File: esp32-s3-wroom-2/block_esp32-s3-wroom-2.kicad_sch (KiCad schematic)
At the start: 11 parts, among them SW1 SW_Push, SW2 SW_Push, U1 ESP32-S3-WROOM-2

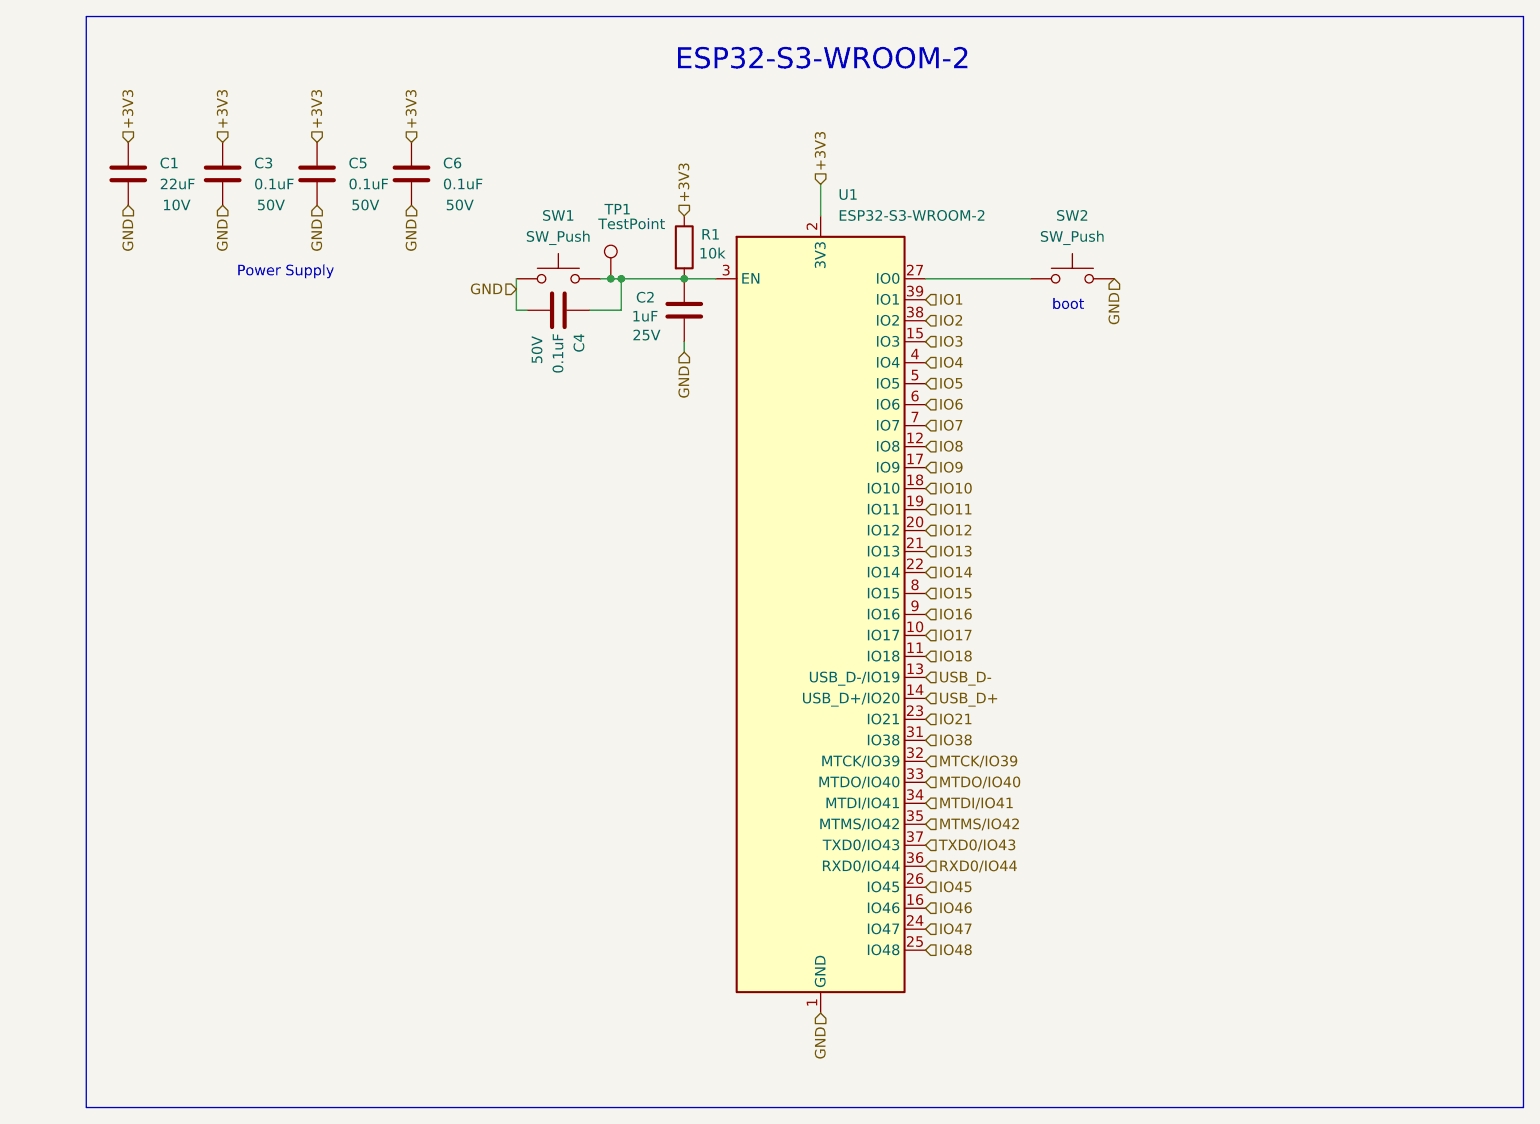
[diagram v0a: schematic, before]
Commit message: [Rushil] corrected pcb added information on both schematic and pcb user drawing correct circuit of bno055
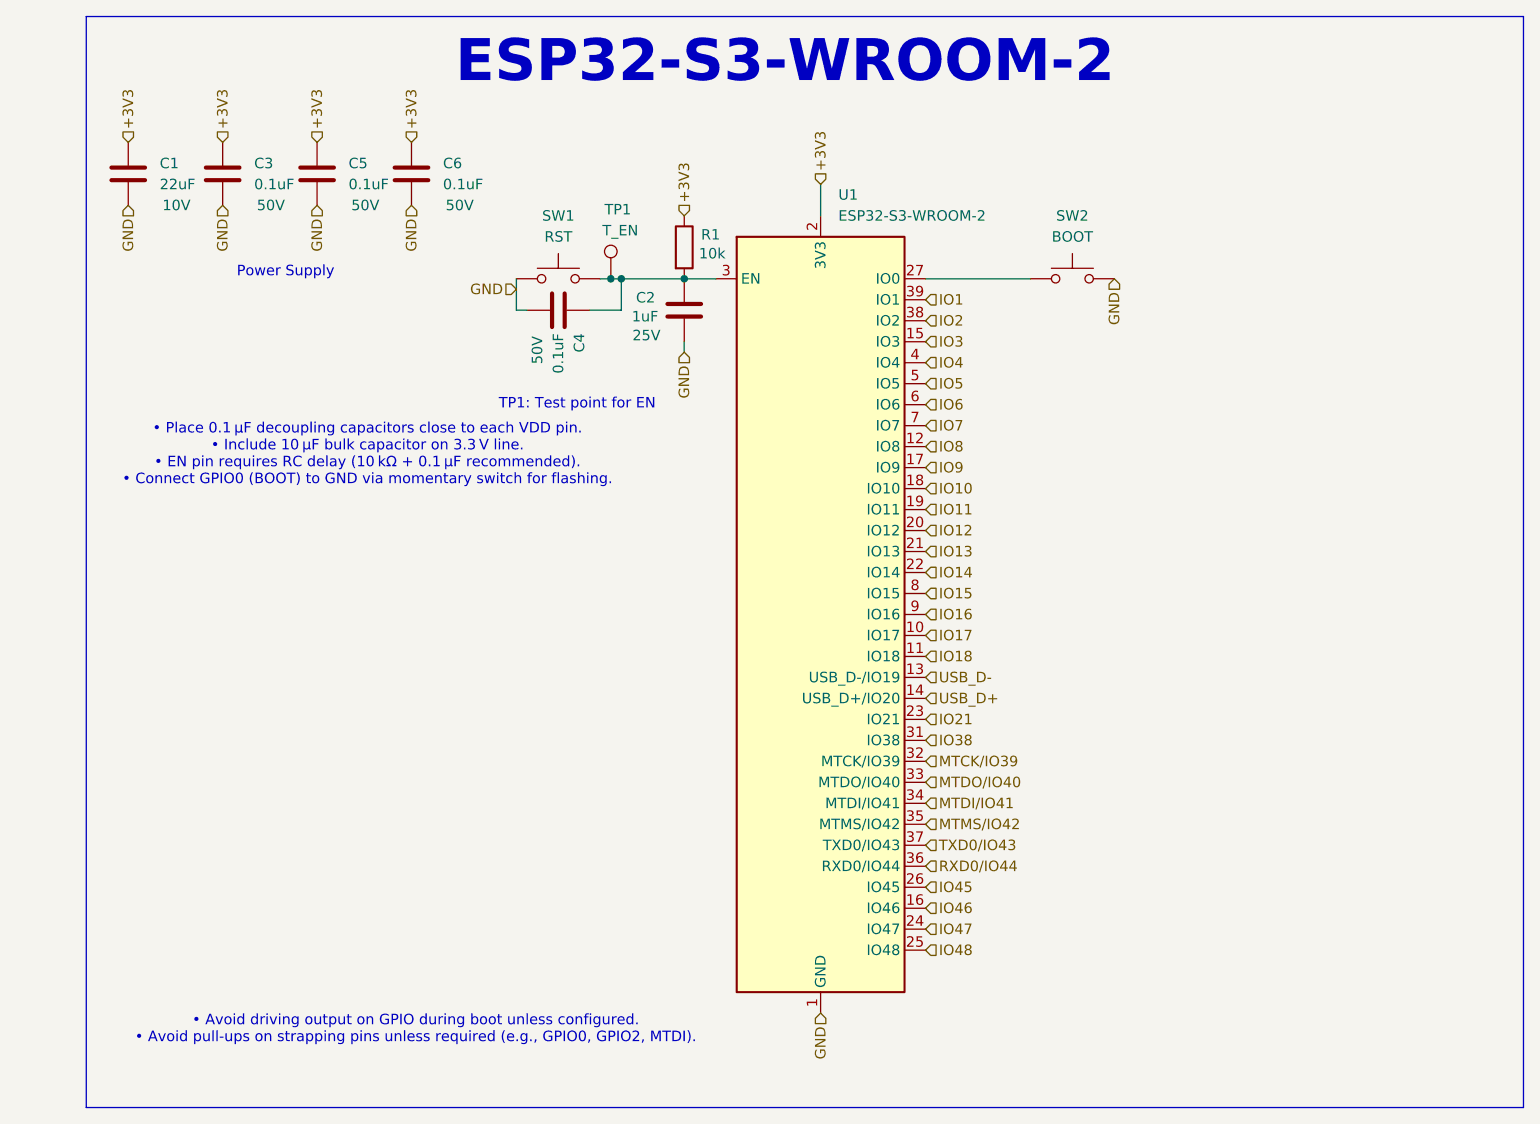
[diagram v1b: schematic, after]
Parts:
- SW1: value SW_Push -> RST
- SW2: value SW_Push -> BOOT
- TP1: value TestPoint -> T_EN
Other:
- note added: "TP1: Test point for EN"
- note added: "• Avoid driving output on GPIO during boot unless configured. • Avoid pull-ups on strapping pins unless required (e.g., GPIO0, GPIO2, MTDI)."
- note added: "• Place 0.1 µF decoupling capacitors close to each VDD pin. • Include 10 µF bulk capacitor on 3.3 V line. • EN pin requires RC delay (10 kΩ + 0.1 µF recommended). • Connect GPIO0 (BOOT) to GND via momentary switch for flashing."
- note removed: "boot"
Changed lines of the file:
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@@
 		)
 	)
-	(text "ESP32-S3-WROOM-2\n"
+	(text "• Place 0.1 µF decoupling capacitors close to each VDD pin.\n• Include 10 µF bulk capacitor on 3.3 V line.\n• EN pin requires RC delay (10 kΩ + 0.1 µF recommended).\n• Connect GPIO0 (BOOT) to GND via momentary switch for flashing.\n"
 		(exclude_from_sim no)
-		(at 151.384 29.464 0)
-		(effects
-			(font
-				(size 2.54 2.54)
-			)
-		)
-	)
-	(text "boot\n"
-		(exclude_from_sim no)
-		(at 181.102 59.182 0)
+		(at 96.266 77.216 0)
 		(effects
 			(font
@@
 			(font
 				(size 1.27 1.27)
+			)
+		)
+	)
+	(text "TP1: Test point for EN"
+		(exclude_from_sim no)
+		(at 121.666 71.12 0)
+		(effects
+			(font
+				(size 1.27 1.27)
+			)
+		)
+	)
+	(text "• Avoid driving output on GPIO during boot unless configured.\n• Avoid pull-ups on strapping pins unless required (e.g., GPIO0, GPIO2, MTDI).\n"
+		(exclude_from_sim no)
+		(at 102.108 146.812 0)
+		(effects
+			(font
+				(size 1.27 1.27)
+			)
+		)
+	)
+	(text "ESP32-S3-WROOM-2\n"
+		(exclude_from_sim no)
+		(at 146.812 29.718 0)
+		(effects
+			(font
+				(size 5.08 5.08)
+				(thickness 1.016)
+				(bold yes)
 			)
 		)
@@
 			)
 		)
-		(property "Value" "TestPoint"
-			(at 124.206 49.276 0)
+		(property "Value" "T_EN"
+			(at 124.714 50.038 0)
 			(effects
 				(font
@@
 			)
 		)
-		(property "Value" "SW_Push"
+		(property "Value" "BOOT"
 			(at 181.61 50.8 0)
 			(effects
@@
 			)
 		)
-		(property "Value" "SW_Push"
+		(property "Value" "RST"
 			(at 119.38 50.8 0)
 			(effects

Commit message: [Rushil] added ams1117-3.3 block and did some clean up in schematic info part
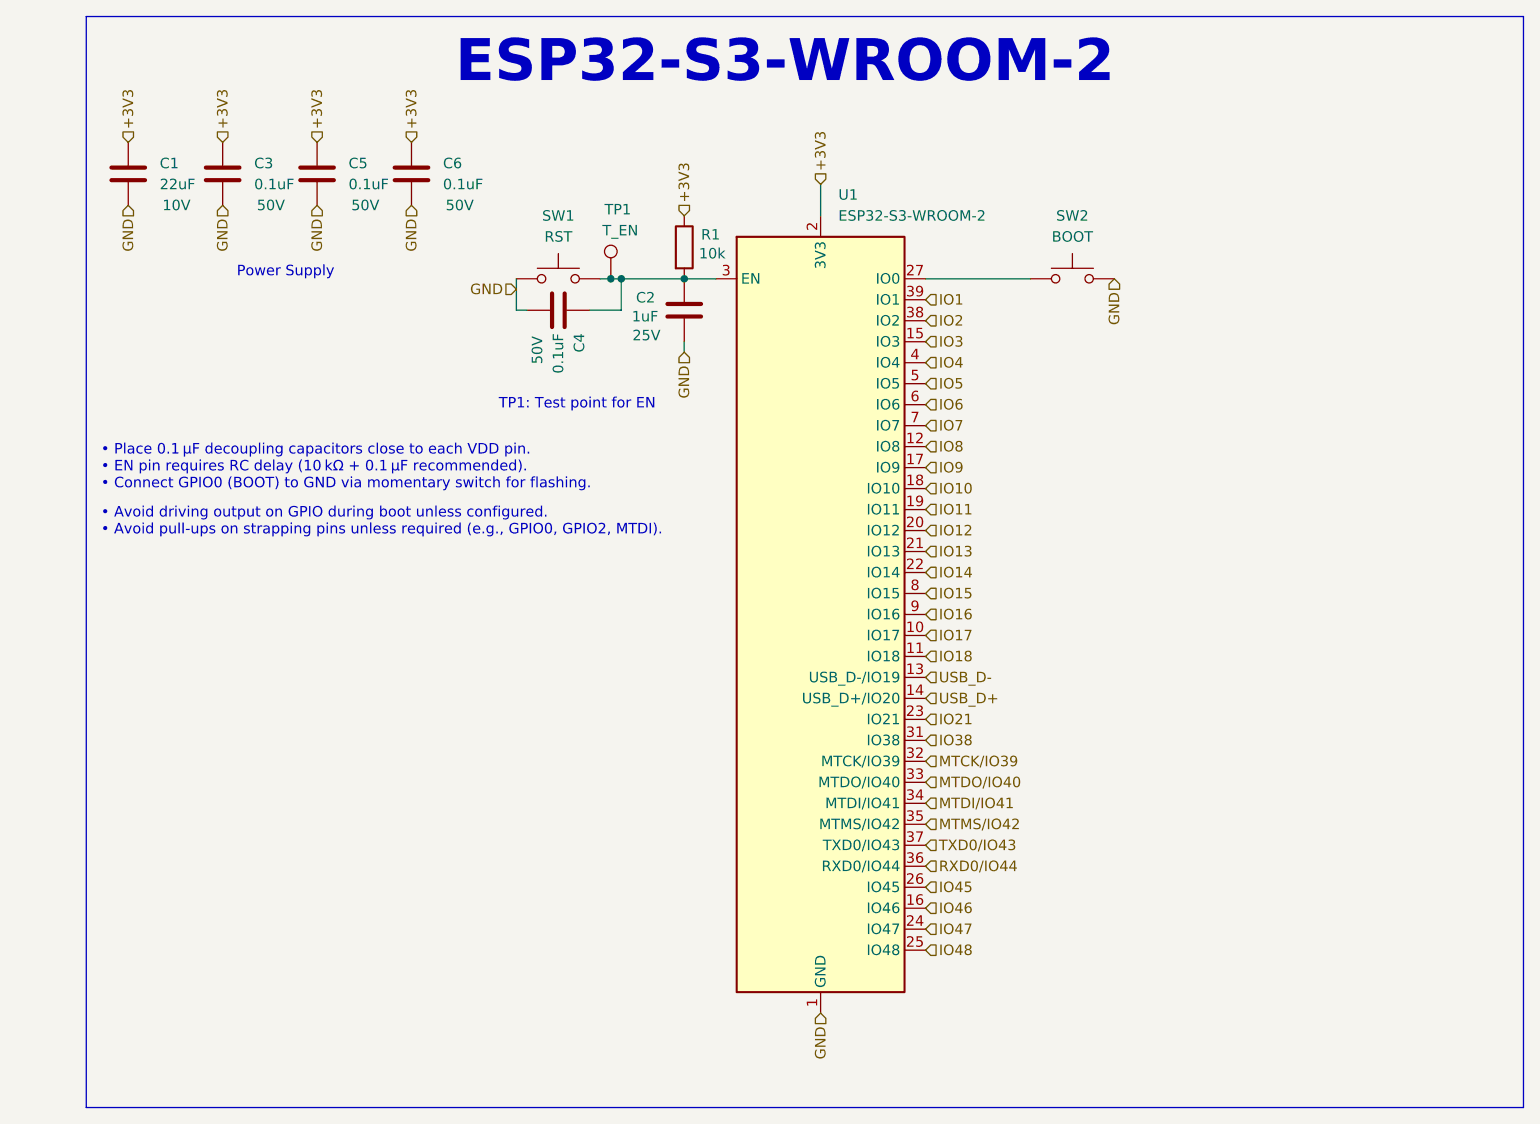
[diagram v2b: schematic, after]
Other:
- note added: "• Place 0.1 µF decoupling capacitors close to each VDD pin. • EN pin requires RC delay (10 kΩ + 0.1 µF recommended). • Connect GPIO0 (BOOT) to GND via momentary switch for flashing."
- note removed: "• Place 0.1 µF decoupling capacitors close to each VDD pin. • Include 10 µF bulk capacitor on 3.3 V line. • EN pin requires RC delay (10 kΩ + 0.1 µF recommended). • Connect GPIO0 (BOOT) to GND via momentary switch for flashing."
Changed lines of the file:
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@@
 		)
 	)
-	(text "• Place 0.1 µF decoupling capacitors close to each VDD pin.\n• Include 10 µF bulk capacitor on 3.3 V line.\n• EN pin requires RC delay (10 kΩ + 0.1 µF recommended).\n• Connect GPIO0 (BOOT) to GND via momentary switch for flashing.\n"
+	(text "• Place 0.1 µF decoupling capacitors close to each VDD pin.\n• EN pin requires RC delay (10 kΩ + 0.1 µF recommended).\n• Connect GPIO0 (BOOT) to GND via momentary switch for flashing.\n"
 		(exclude_from_sim no)
-		(at 96.266 77.216 0)
+		(at 64.008 78.74 0)
 		(effects
 			(font
 				(size 1.27 1.27)
 			)
+			(justify left)
 		)
 	)
@@
 	(text "• Avoid driving output on GPIO during boot unless configured.\n• Avoid pull-ups on strapping pins unless required (e.g., GPIO0, GPIO2, MTDI).\n"
 		(exclude_from_sim no)
-		(at 102.108 146.812 0)
+		(at 64.008 85.344 0)
 		(effects
 			(font
 				(size 1.27 1.27)
 			)
+			(justify left)
 		)
 	)

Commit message: [Rushil] fixed block esp32 wroom
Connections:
- net +3V3 renamed 3V3
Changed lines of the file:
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@@
 		)
 	)
-	(hierarchical_label "+3V3"
+	(hierarchical_label "3V3"
 		(shape input)
 		(at 78.74 39.37 90)
@@
 		)
 	)
-	(hierarchical_label "+3V3"
+	(hierarchical_label "3V3"
 		(shape input)
 		(at 151.13 44.45 90)
@@
 		)
 	)
-	(hierarchical_label "+3V3"
+	(hierarchical_label "3V3"
 		(shape input)
 		(at 67.31 39.37 90)
@@
 		)
 	)
-	(hierarchical_label "+3V3"
+	(hierarchical_label "3V3"
 		(shape input)
 		(at 90.17 39.37 90)
@@
 		)
 	)
-	(hierarchical_label "+3V3"
+	(hierarchical_label "3V3"
 		(shape input)
 		(at 101.6 39.37 90)
@@
 		)
 	)
-	(hierarchical_label "+3V3"
+	(hierarchical_label "3V3"
 		(shape input)
 		(at 134.62 48.26 90)

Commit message: [Rushil] small changes in  esp32 wroom
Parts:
- U1: LCSC_part# (none) -> C3021270; MPN (none) -> ESP32-S3-WROOM-2-N32R8V
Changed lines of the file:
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@@
+			)
+		)
+		(property "LCSC_part#" "C3021270"
+			(at 151.13 96.52 0)
+			(effects
+				(font
+					(size 1.27 1.27)
+				)
+				(hide yes)
+			)
+		)
+		(property "MPN" "ESP32-S3-WROOM-2-N32R8V"
+			(at 151.13 96.52 0)
+			(effects
+				(font
+					(size 1.27 1.27)
+				)
+				(hide yes)
 			)
 		)
